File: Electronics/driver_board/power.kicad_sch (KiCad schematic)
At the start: 15 parts, among them U5 TPS4810-Q1, U6 LMW78_12-0.5R, U7 REF3433TIDBVR

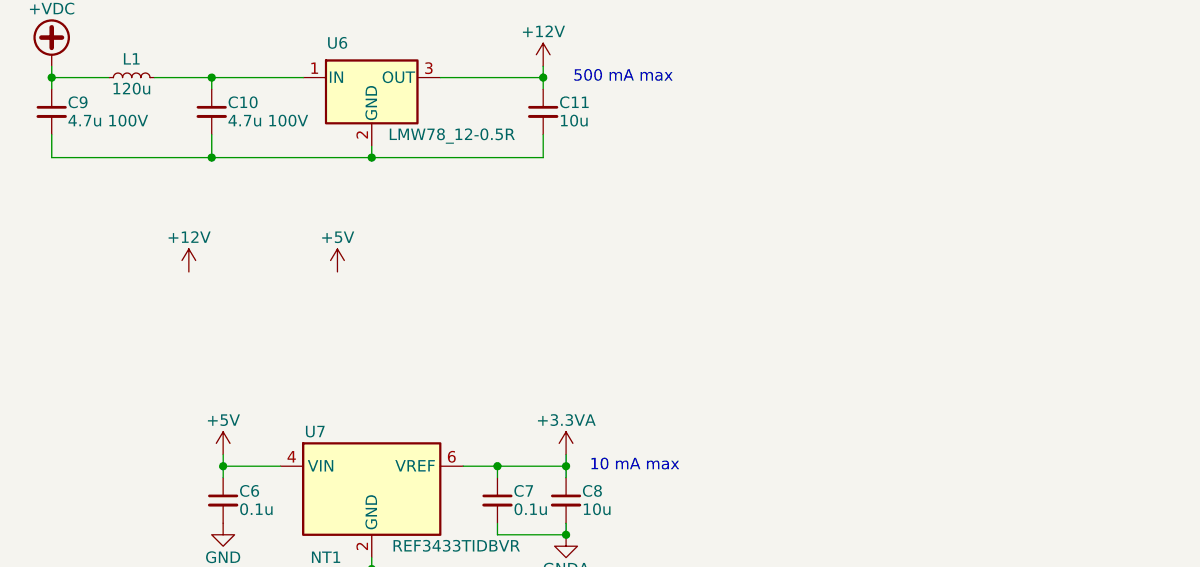
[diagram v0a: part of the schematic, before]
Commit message: [pcb] Added regulators, pin mapping
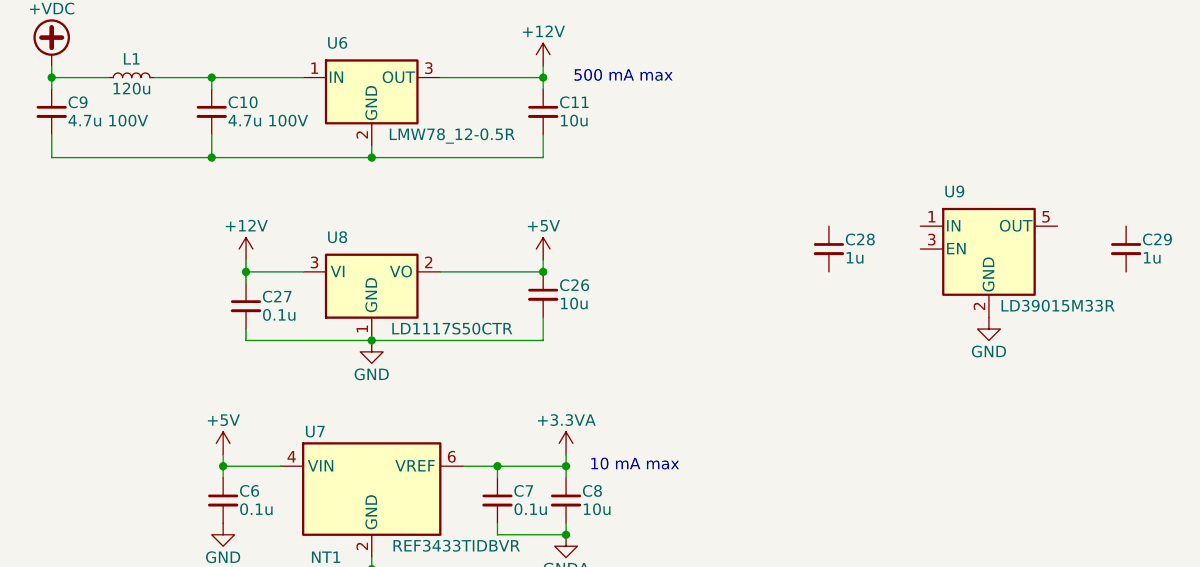
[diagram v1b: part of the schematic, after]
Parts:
- added C26: 10u, symbol Device:C_Small
- added C27: 0.1u, symbol Device:C_Small
- added C28, C29: 1u, symbol Device:C_Small
- added U8: LD1117S50CTR, Package_TO_SOT_SMD:SOT-223-3_TabPin2, symbol Regulator_Linear:LD1117S50TR_SOT223
- added U9: LD39015M33R, Package_TO_SOT_SMD:SOT-23-5, symbol Regulator_Linear:LD39015M33R
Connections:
- net +12V: now also C27.1, U8.3 (VI)
- net +5V: now also C26.1, U8.2 (VO)
- net GND: now also C26.2, C27.2, U8.1 (GND), U9.2 (GND)

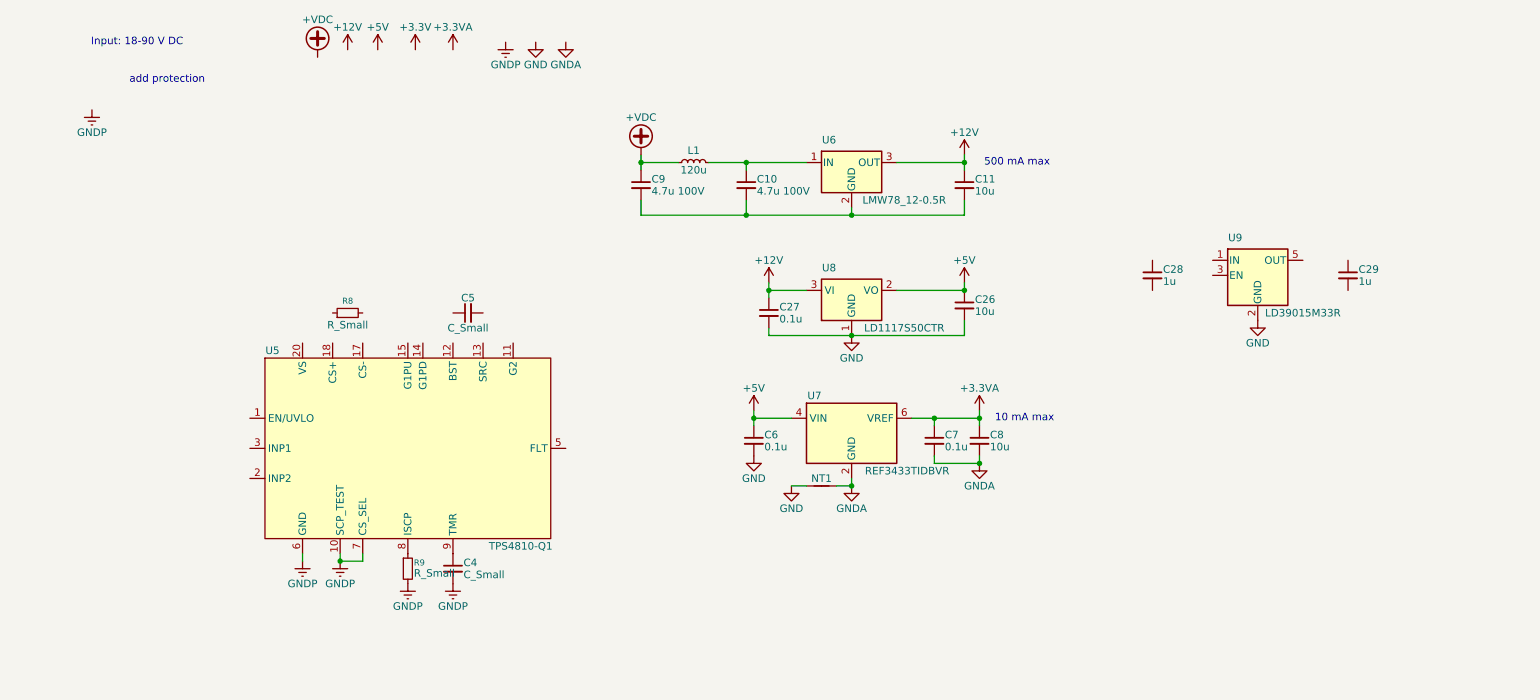
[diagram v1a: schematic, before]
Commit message: [pcb] Populating efuse parts
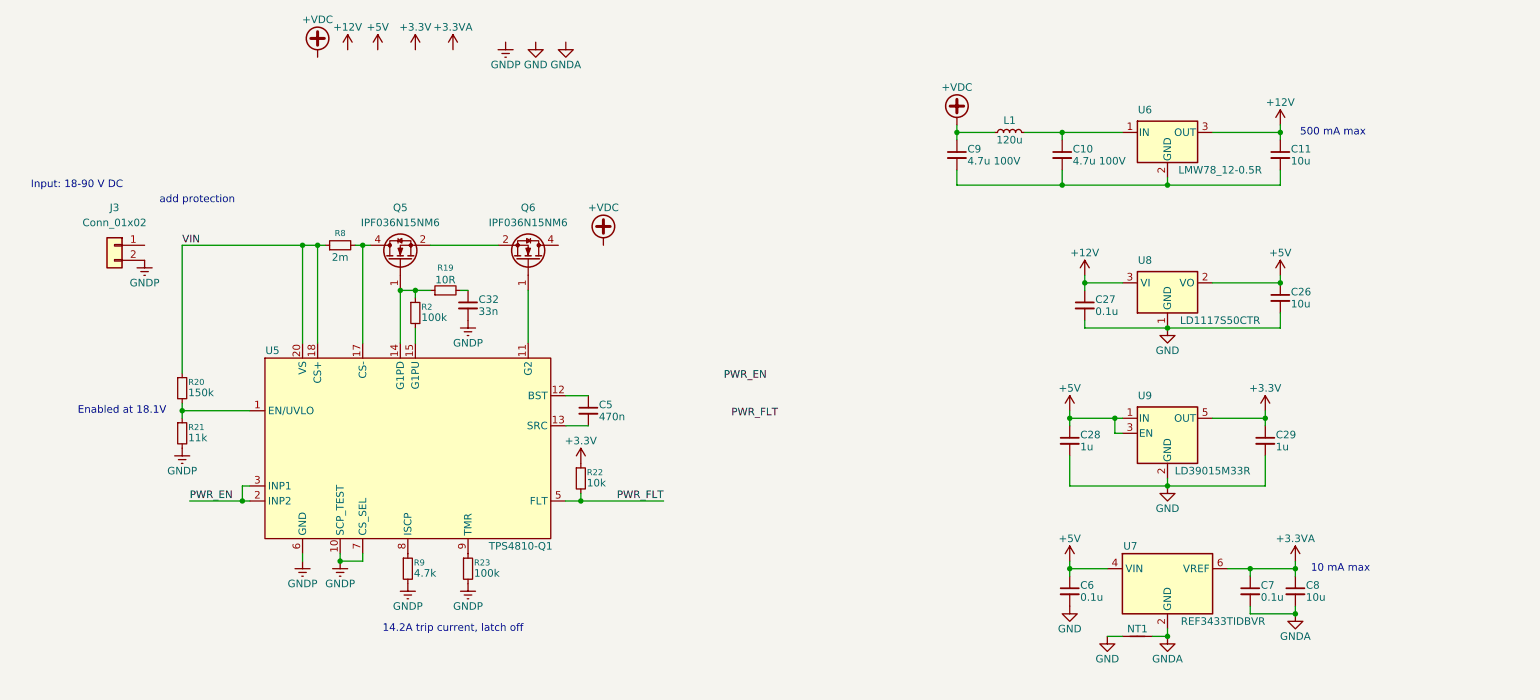
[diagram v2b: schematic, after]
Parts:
- removed C4: C_Small, symbol Device:C_Small
- added C32: 33n, symbol Device:C_Small
- added J3: Conn_01x02, symbol Connector_Generic:Conn_01x02
- added Q5, Q6: IPF036N15NM6, Package_TO_SOT_SMD:TO-263-6, symbol DWlib:IPF036N15NM6
- added R19: 10R, symbol Device:R_Small
- added R2, R23: 100k, symbol Device:R_Small
- added R20: 150k, symbol Device:R_Small
- added R21: 11k, symbol Device:R_Small
- added R22: 10k, symbol Device:R_Small
- C5: value C_Small -> 470n
- R8: value R_Small -> 2m
- R9: value R_Small -> 4.7k
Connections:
- net +3.3V: now also C29.1, U9.5 (OUT), R22.1
- net +5V: now also C28.1, U9.1 (IN), U9.3 (EN)
- net GND: now also C28.2, C29.2
- net GNDP: now also C32.2, J3.2 (Pin_2), R21.2, R23.2
- net at U5.1 (EN/UVLO): now also R20.2, R21.1
- net at U5.11 (G2): now also Q6.1 (G)
- net at U5.12 (BST): now also C5.1
- net at U5.13 (SRC): now also C5.2
- net at U5.14 (G1PD): now also Q5.1 (G), R19.1, R2.1
- net at U5.15 (G1PU): now also R2.2
- net at U5.17 (CS-): now also R8.2, Q5.4 (D)
- net VIN: now reaches U5.18 (CS+)
- net VIN: now also R8.1, U5.20 (VS), R20.1
- net PWR_EN: now reaches U5.2 (INP2)
- net PWR_EN: now also U5.3 (INP1)
- net PWR_FLT: now reaches U5.5 (FLT)
- net PWR_FLT: now also R22.2
- net at U5.9 (TMR): now also R23.1
- new net: C32.1, R19.2
- new net: Q5.2 (S), Q5.3 (S), Q5.5 (S), Q5.6 (S), Q5.7 (S), Q6.2 (S), Q6.3 (S), Q6.5 (S), Q6.6 (S), Q6.7 (S)
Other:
- note added: "14.2A trip current, latch off"
- note added: "Enabled at 18.1V"
- moved on the sheet: C10, C11, C26, C27, C28, C29, C6, C7, C8, C9, L1, NT1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

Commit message: Added TVS diodes, bulk capacitors
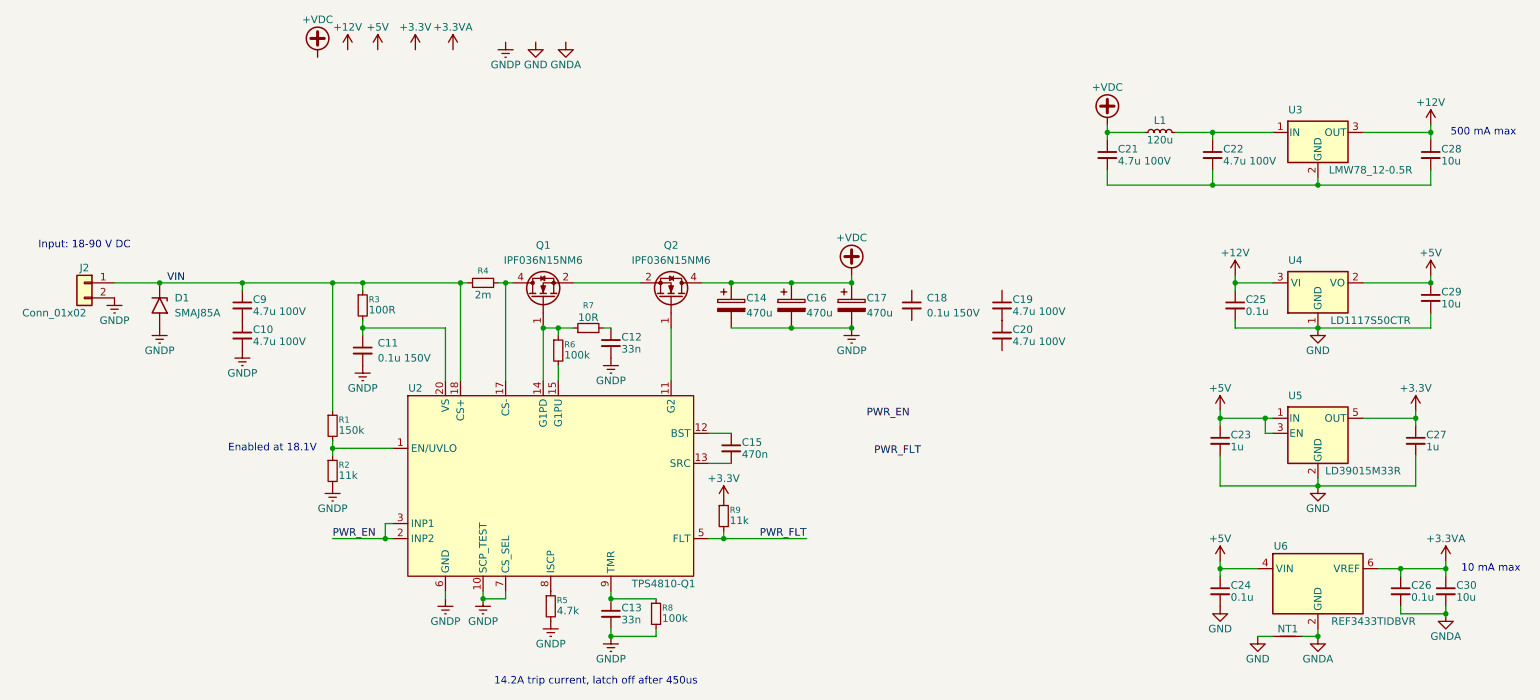
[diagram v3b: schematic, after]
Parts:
- added C10, C19, C20, C9: 4.7u 100V, symbol Device:C_Small
- added C11, C18: 0.1u 150V, Capacitor_SMD:C_0805_2012Metric, symbol Device:C_Small
- added C13: 33n, symbol Device:C_Small
- added C14, C16, C17: 470u, symbol Device:C_Polarized
- added D1: SMAJ85A, Diode_SMD:D_SMA, symbol Diode:SMAJ85A
- added R3: 100R, Resistor_SMD:R_0603_1608Metric, symbol Device:R_Small
- C23: renamed from C28; footprint (none) -> Capacitor_SMD:C_0402_1005Metric
- C24: renamed from C6; footprint (none) -> Capacitor_SMD:C_0402_1005Metric
- C25: renamed from C27; footprint (none) -> Capacitor_SMD:C_0402_1005Metric
- C26: renamed from C7; footprint (none) -> Capacitor_SMD:C_0402_1005Metric
- C27: renamed from C29; footprint (none) -> Capacitor_SMD:C_0402_1005Metric
- C28: renamed from C11; footprint (none) -> Capacitor_SMD:C_0805_2012Metric
- C29: renamed from C26; footprint (none) -> Capacitor_SMD:C_0805_2012Metric
- C30: renamed from C8; footprint (none) -> Capacitor_SMD:C_0805_2012Metric
- R1: renamed from R20; footprint (none) -> Resistor_SMD:R_0603_1608Metric
- R2: renamed from R21; footprint (none) -> Resistor_SMD:R_0603_1608Metric
- R4: renamed from R8; footprint (none) -> Resistor_SMD:R_1206_3216Metric
- R5: renamed from R9; footprint (none) -> Resistor_SMD:R_0603_1608Metric
- R6: renamed from R2; footprint (none) -> Resistor_SMD:R_0603_1608Metric
- R7: renamed from R19; footprint (none) -> Resistor_SMD:R_0603_1608Metric
- R8: renamed from R23; footprint (none) -> Resistor_SMD:R_0603_1608Metric
- R9: renamed from R22; value 10k -> 11k; footprint (none) -> Resistor_SMD:R_0603_1608Metric
- renumbered C32 to C12, C5 to C15, C9 to C21, C10 to C22, J3 to J2, Q5 to Q1, Q6 to Q2, U5 to U2, U6 to U3, U8 to U4, U9 to U5, U7 to U6
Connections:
- net +VDC: now also Q2.4 (D), C14.1, C16.1, C17.1
- net GNDP: now also C10.2, C11.2, C13.2, C14.2, C16.2, C17.2, D1.2 (A2)
- net VIN: now also J2.1 (Pin_1), C9.1, D1.1 (A1), R3.1; no longer U2.20 (VS)
- net at R8.1, U2.9 (TMR): now also C13.1
- new net: C11.1, R3.2, U2.20 (VS)
- new net: C19.2, C20.1
- new net: C10.1, C9.2
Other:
- note added: "14.2A trip current, latch off after 450us"
- note removed: "14.2A trip current, latch off"
- note removed: "add protection"
- moved on the sheet: C12, C15, C21, C22, C23, C24, C25, C26, C27, C28, C29, C30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
